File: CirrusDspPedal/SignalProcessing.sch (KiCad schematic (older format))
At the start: 8 parts, among them J3 Conn_02x05_Odd_Even, U4 STM32F411RETx

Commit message: Added Footswitches and relay
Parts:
- J3: footprint (none) -> Connector_PinHeader_2.54mm:PinHeader_2x05_P2.54mm_Vertical_SMD
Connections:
- net labels added: ExpInput, FootSwitchA, FootSwitchB, SIgnalSwitch
- wire segments 84 -> 90
- no-connect marks 44 -> 40
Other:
- moved on the sheet: C18, C19, C20, C21, C22, J3, L1

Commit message: Added UserPots and RGB LEDS
Updated schema docs
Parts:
- added LED1, LED2: LED_RABG, LED_THT:LED_D5.0mm-4_RGB_Wide_Pins, symbol Device:LED_RABG
- added R17, R18, R19, R20, R21, R22: 220R, Resistor_SMD:R_0805_2012Metric_Pad1.15x1.40mm_HandSolder, symbol Device:R
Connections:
- net labels added: LEDA_B, LEDA_G, LEDA_R, LEDB_B, LEDB_G, LEDB_R, UserPotA, UserPotB, UserSwA, UserSwB
- wire segments 90 -> 116
- no-connect marks 40 -> 30
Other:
- note added: "I2S_2_CK"
- note added: "I2S_2_Ext_SD"
- note added: "I2S_2_MCLK"
- note added: "I2S_2_SD"
- note added: "I2S_2_WS"
- moved on the sheet: C18, C19, C20, C21, C22, J3, L1

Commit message: Completed schematic design
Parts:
- removed U4: STM32F411RETx, Package_QFP:LQFP-64_10x10mm_P0.5mm, symbol MCU_ST_STM32F4:STM32F411RETx
- added C33: 2.2uF, Capacitor_SMD:C_0805_2012Metric_Pad1.15x1.40mm_HandSolder, symbol Device:C
- added U7: STM32F405RGTx, Package_QFP:LQFP-64_10x10mm_P0.5mm, symbol MCU_ST_STM32F4:STM32F405RGTx
- C22: value 100nF -> 2.2uF
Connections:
- net labels added: FootExp_IN, FootSwitchA_IN, FootSwitchB_IN, RelayCoil_OUT, UserPotA_IN, UserPotB_IN, UserSwitchB_IN, UserSwithA_IN, VCAP1, VCAP2, uSD_CLK, uSD_CMD, uSD_D0, uSD_D1, uSD_D2, uSD_D3, uSD_Detect
- net labels removed: ExpInput, FootSwitchA, FootSwitchB, SIgnalSwitch, UserPotA, UserPotB, UserSwA, UserSwB
- wire segments 116 -> 125
- no-connect marks 30 -> 24
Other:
- note added: "AnalogInput"
- note added: "DigitalInput"
- note added: "DigitalOutput"
- note added: "SDIO_CK"
- note added: "SDIO_CMD"
- note added: "SDIO_D0"
- note added: "SDIO_D1"
- note added: "SDIO_D2"
- note added: "SDIO_D3"
- note added: "SDIO_Detect"
- note added: "SYS_JTCK-SWCLK"
- note added: "SYS_JTDO-SWO"
- note added: "SYS_JTMS-SWDIO"
- moved on the sheet: C22

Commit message: updates
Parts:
- J3: footprint Connector_PinHeader_2.54mm:PinHeader_2x05_P2.54mm_Vertical_SMD -> Connector_PinHeader_1.27mm:PinHeader_2x05_P1.27mm_Vertical_SMD
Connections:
- net labels removed: VBAT
- wire segments 125 -> 121
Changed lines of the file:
@@
 $Descr A4 11693 8268
 encoding utf-8
-Sheet 8 11
+Sheet 8 10
 Title ""
 Date ""
@@
 Wire Wire Line
 	6350 1600 6350 1325
-Text Label 6125 1325 0    50   ~ 0
-VBAT
 Wire Wire Line
 	6600 1325 6600 1150
@@
 Wire Wire Line
 	5850 2000 4950 2000
-$Sheet
-S 1850 925  925  625
-U 5F89A953
-F0 "STM32F411_PowerFiltering" 50
-F1 "STM32F411_PowerFiltering.sch" 50
-F2 "VDDA" I R 2775 1125 50
-F3 "VBAT" I R 2775 1350 50
-F4 "VDD_IN" I L 1850 1125 50
-$EndSheet
-Text Label 3425 1350 0    50   ~ 0
-VBAT
-Wire Wire Line
-	2775 1350 3425 1350
-Text Label 3425 1125 0    50   ~ 0
-VDDA
-Wire Wire Line
-	2775 1125 3425 1125
-$Comp
-L power:+3.3V #PWR0118
-U 1 1 5F8C8E66
-P 1400 1000
-F 0 "#PWR0118" H 1400 850 50  0001 C CNN
-F 1 "+3.3V" H 1415 1173 50  0000 C CNN
-F 2 "" H 1400 1000 50  0001 C CNN
-F 3 "" H 1400 1000 50  0001 C CNN
-	1    1400 1000
-	1    0    0    -1
-$EndComp
-Wire Wire Line
-	1400 1125 1400 1000
-Wire Wire Line
-	1850 1125 1400 1125
 $Comp
 L Device:C C?
@@
 F 0 "J3" H 2375 3017 50  0000 C CNN
 F 1 "Conn_02x05_Odd_Even" H 2375 2926 50  0000 C CNN
-F 2 "Connector_PinHeader_2.54mm:PinHeader_2x05_P2.54mm_Vertical_SMD" H 2325 2600 50  0001 C CNN
-F 3 "~" H 2325 2600 50  0001 C CNN
+F 2 "Connector_PinHeader_1.27mm:PinHeader_2x05_P1.27mm_Vertical_SMD" H 2325 2600 50  0001 C CNN
+F 3 "https://docs.rs-online.com/75e3/0900766b8142184e.pdf" H 2325 2600 50  0001 C CNN
 	1    2325 2600
 	1    0    0    -1
@@
 	6850 1325 7075 1325
 Wire Wire Line
-	6350 1325 6125 1325
+	6350 1325 6450 1325
 Wire Wire Line
 	7250 1800 7950 1800
@@
 Text Notes 7375 2600 0    50   ~ 0
 SDIO_Detect
+Connection ~ 6450 1325
 $EndSCHEMATC

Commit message: updated design and layout
- Changed LDO to 1703 (footprint unchanged)
- Changed THT LEDs from RAGB (incorrect) to RCGB (correct) symbol (footprint unchanged)
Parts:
- removed LED1, LED2: LED_RABG, LED_THT:LED_D5.0mm-4_RGB_Wide_Pins, symbol Device:LED_RABG
- added LED1, LED2: LED_RCBG, LED_THT:LED_D5.0mm-4_RGB_Wide_Pins, symbol Device:LED_RCBG
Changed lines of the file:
@@
 Text HLabel 7950 2000 2    50   Input ~ 0
 UserPotB_IN
-$Comp
-L Device:LED_RABG LED1
-U 1 1 5F968A63
-P 10000 2450
-F 0 "LED1" H 10000 2947 50  0000 C CNN
-F 1 "LED_RABG" H 10000 2856 50  0000 C CNN
-F 2 "LED_THT:LED_D5.0mm-4_RGB_Wide_Pins" H 10000 2400 50  0001 C CNN
-F 3 "~" H 10000 2400 50  0001 C CNN
-	1    10000 2450
-	1    0    0    -1
-$EndComp
 Wire Wire Line
 	9800 2250 9700 2250
@@
 Text Label 9050 2650 0    50   ~ 0
 LEDA_B
-$Comp
-L Device:LED_RABG LED2
-U 1 1 5F8E8343
-P 10000 3650
-F 0 "LED2" H 10000 4147 50  0000 C CNN
-F 1 "LED_RABG" H 10000 4056 50  0000 C CNN
-F 2 "LED_THT:LED_D5.0mm-4_RGB_Wide_Pins" H 10000 3600 50  0001 C CNN
-F 3 "~" H 10000 3600 50  0001 C CNN
-	1    10000 3650
-	1    0    0    -1
-$EndComp
 Wire Wire Line
 	9800 3450 9700 3450
@@
 SDIO_Detect
 Connection ~ 6450 1325
+$Comp
+L Device:LED_RCBG LED1
+U 1 1 5F9CA392
+P 10000 2450
+F 0 "LED1" H 10000 2947 50  0000 C CNN
+F 1 "LED_RCBG" H 10000 2856 50  0000 C CNN
+F 2 "LED_THT:LED_D5.0mm-4_RGB_Wide_Pins" H 10000 2400 50  0001 C CNN
+F 3 "~" H 10000 2400 50  0001 C CNN
+	1    10000 2450
+	-1   0    0    -1
+$EndComp
+$Comp
+L Device:LED_RCBG LED2
+U 1 1 5F9CDB3E
+P 10000 3650
+F 0 "LED2" H 10000 4147 50  0000 C CNN
+F 1 "LED_RCBG" H 10000 4056 50  0000 C CNN
+F 2 "LED_THT:LED_D5.0mm-4_RGB_Wide_Pins" H 10000 3600 50  0001 C CNN
+F 3 "~" H 10000 3600 50  0001 C CNN
+	1    10000 3650
+	-1   0    0    -1
+$EndComp
 $EndSCHEMATC

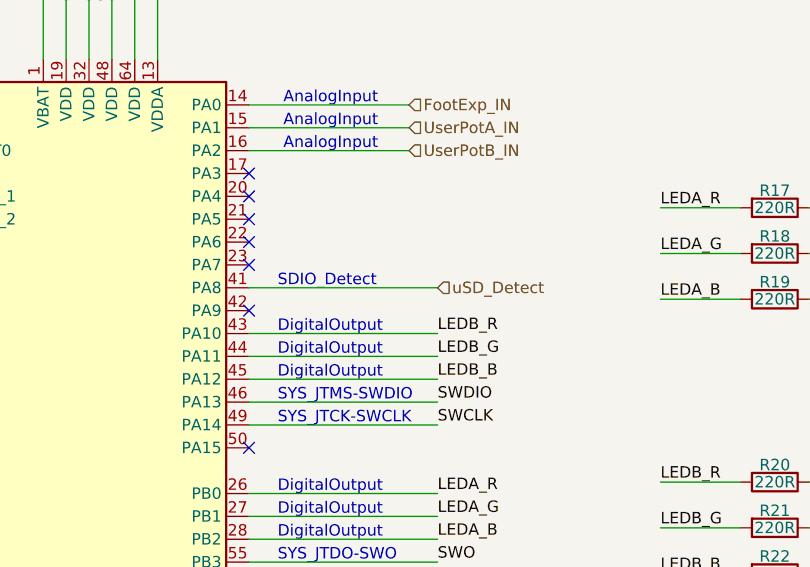
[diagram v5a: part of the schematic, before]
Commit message: replaced SDIO connector
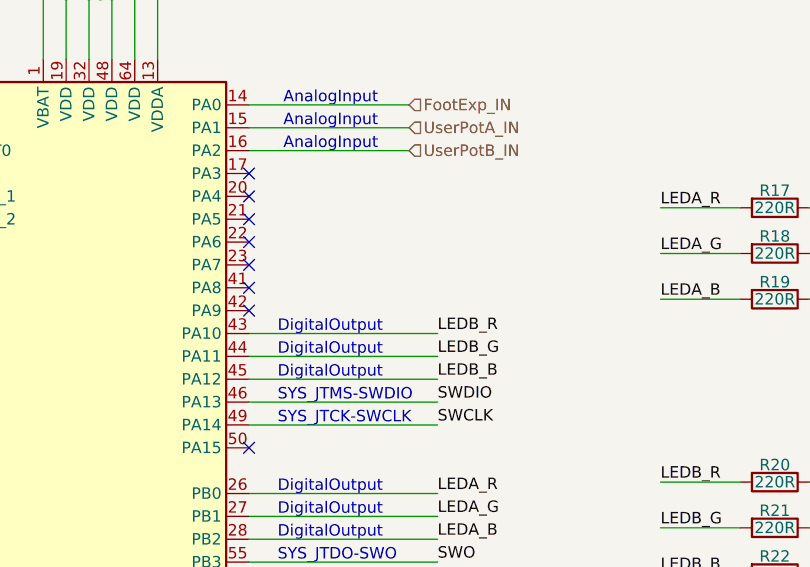
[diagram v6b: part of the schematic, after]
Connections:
- net uSD_Detect: no longer names the net of U7.41 (PA8)
- no-connect marks 24 -> 25
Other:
- note removed: "SDIO_Detect"
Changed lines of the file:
@@
 Text HLabel 5100 4600 0    50   Input ~ 0
 uSD_D3
-Wire Wire Line
-	7250 2600 8075 2600
-Text HLabel 8075 2600 2    50   Input ~ 0
-uSD_Detect
-Text Notes 7375 2600 0    50   ~ 0
-SDIO_Detect
 Connection ~ 6450 1325
 $Comp
@@
 	-1   0    0    -1
 $EndComp
+NoConn ~ 7250 2600
 $EndSCHEMATC

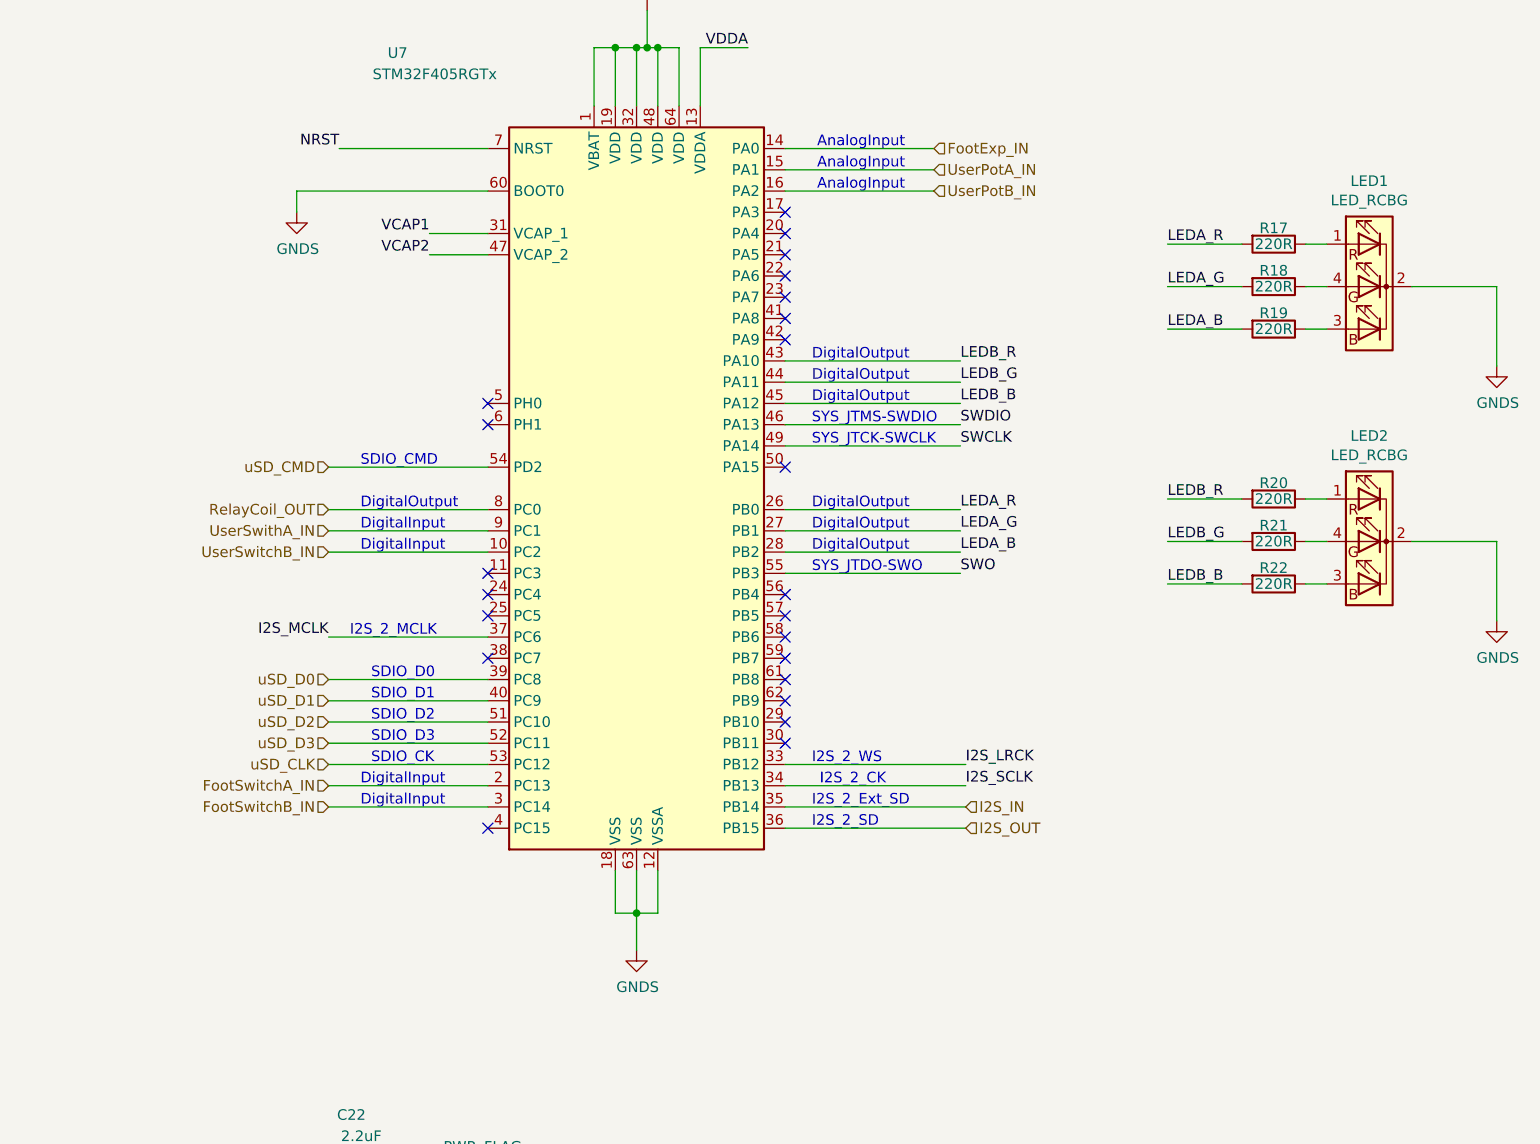
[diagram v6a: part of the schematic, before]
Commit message: Updated RevB
- Replaced analog pots with Rotary Encoders
- Added I2C connector (for OLED screen)
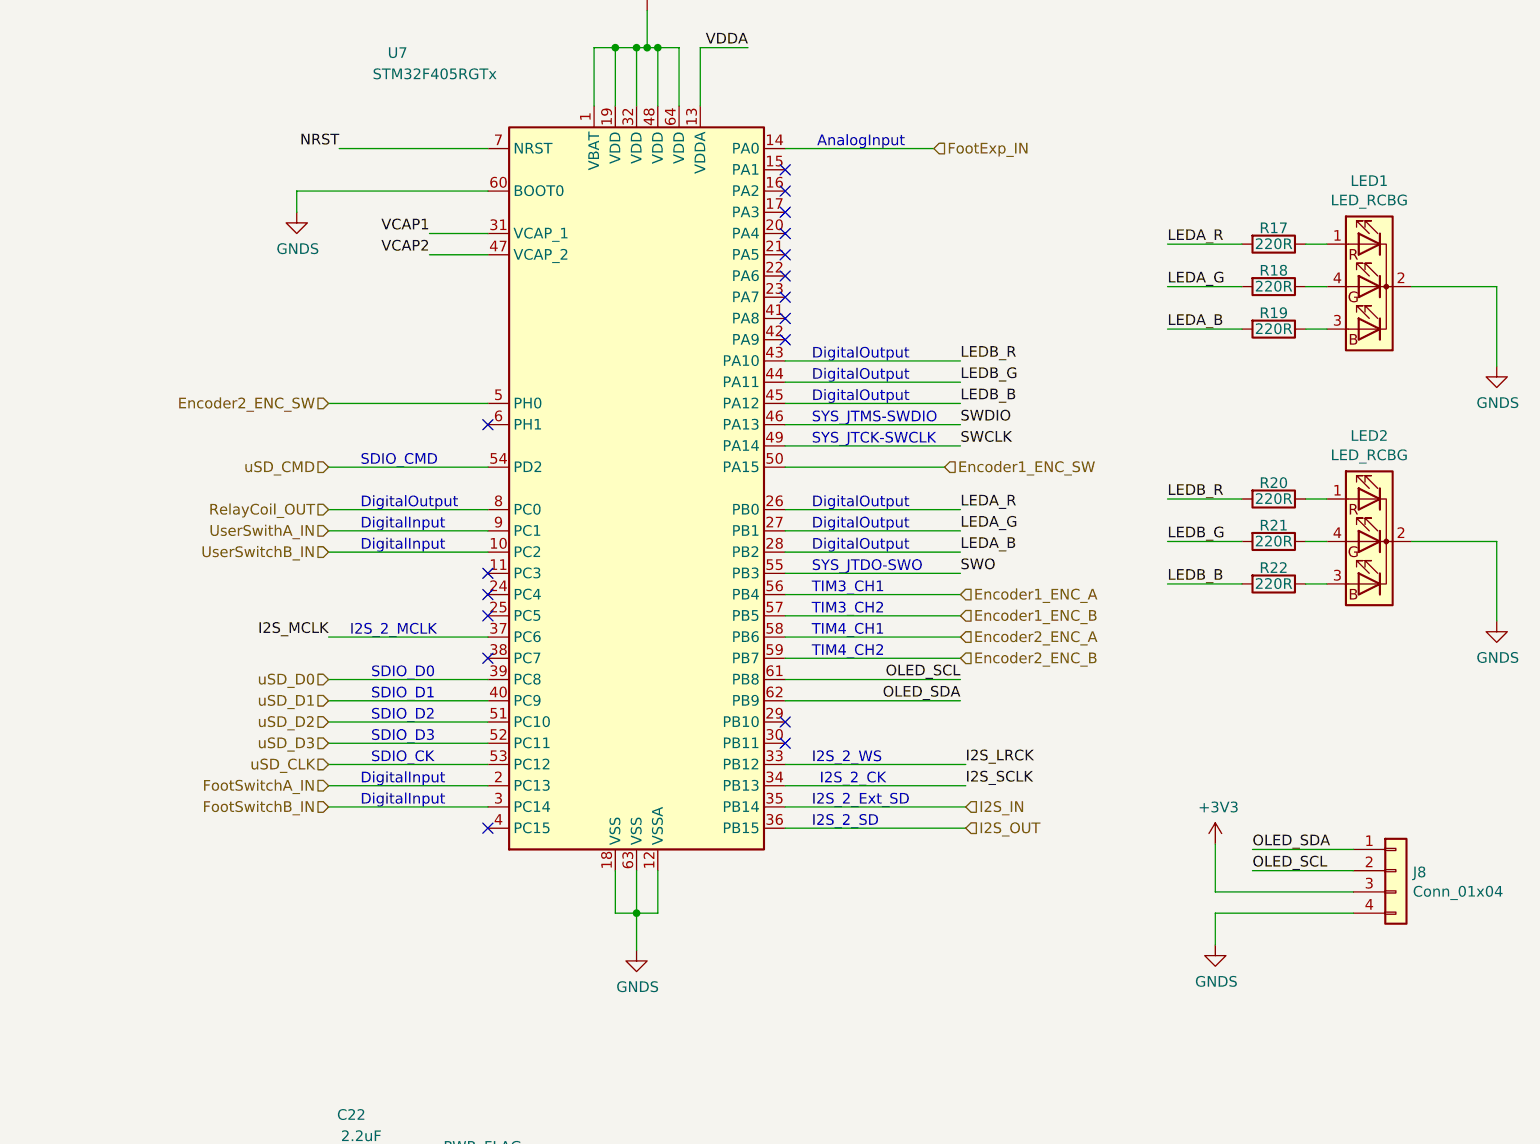
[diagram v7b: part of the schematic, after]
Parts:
- added J8: Conn_01x04, Connector_Molex:Molex_KK-254_AE-6410-04A_1x04_P2.54mm_Vertical, symbol Connector_Generic:Conn_01x04
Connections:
- net +3V3: now also J8.3 (Pin_3)
- net GNDS: now also J8.4 (Pin_4)
- net Encoder2_ENC_SW: now reaches U7.5 (PH0)
- net Encoder1_ENC_SW: now reaches U7.50 (PA15)
- net Encoder1_ENC_A: now reaches U7.56 (PB4)
- net Encoder1_ENC_B: now reaches U7.57 (PB5)
- net Encoder2_ENC_A: now reaches U7.58 (PB6)
- net Encoder2_ENC_B: now reaches U7.59 (PB7)
- net OLED_SCL: now reaches U7.61 (PB8)
- net OLED_SCL: now also J8.2 (Pin_2)
- net OLED_SDA: now reaches U7.62 (PB9)
- net OLED_SDA: now also J8.1 (Pin_1)
- net UserPotA_IN: no longer names the net of U7.15 (PA1)
- net UserPotB_IN: no longer names the net of U7.16 (PA2)
- no-connect marks 25 -> 19
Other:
- note added: "TIM3_CH1"
- note added: "TIM3_CH2\n"
- note added: "TIM4_CH1"
- note added: "TIM4_CH2"
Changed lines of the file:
@@
 $Descr A4 11693 8268
 encoding utf-8
-Sheet 8 10
+Sheet 8 12
 Title ""
 Date ""
@@
 Text HLabel 2725 3800 2    50   Input ~ 0
 I2S_SCLK_OUT
-NoConn ~ 5850 3000
 NoConn ~ 5850 3900
 NoConn ~ 5850 4000
 NoConn ~ 7250 4500
 NoConn ~ 5850 3800
-NoConn ~ 7250 4400
-NoConn ~ 7250 4300
-NoConn ~ 7250 4200
-NoConn ~ 7250 4100
-NoConn ~ 7250 4000
-NoConn ~ 7250 3900
-NoConn ~ 7250 3300
 NoConn ~ 7250 2700
 NoConn ~ 7250 2500
@@
 Text HLabel 7950 1800 2    50   Input ~ 0
 FootExp_IN
-Wire Wire Line
-	7250 1900 7950 1900
-Text HLabel 7950 1900 2    50   Input ~ 0
-UserPotA_IN
-Wire Wire Line
-	7250 2000 7950 2000
-Text HLabel 7950 2000 2    50   Input ~ 0
-UserPotB_IN
 Wire Wire Line
 	9800 2250 9700 2250
@@
 DigitalInput
 Text Notes 7400 1800 0    50   ~ 0
-AnalogInput
-Text Notes 7400 1900 0    50   ~ 0
-AnalogInput
-Text Notes 7400 2000 0    50   ~ 0
 AnalogInput
 Text Notes 7375 2800 0    50   ~ 0
@@
 $EndComp
 NoConn ~ 7250 2600
+Wire Wire Line
+	7250 3900 8075 3900
+Text HLabel 8075 3900 2    50   Input ~ 0
+Encoder1_ENC_A
+Text Notes 7375 3900 0    50   ~ 0
+TIM3_CH1
+Text Notes 7375 4000 0    50   ~ 0
+TIM3_CH2\n
+Wire Wire Line
+	7250 4000 8075 4000
+Text HLabel 8075 4000 2    50   Input ~ 0
+Encoder1_ENC_B
+Wire Wire Line
+	7250 4100 8075 4100
+Wire Wire Line
+	7250 4200 8075 4200
+Text Notes 7375 4100 0    50   ~ 0
+TIM4_CH1
+Text Notes 7375 4200 0    50   ~ 0
+TIM4_CH2
+Text HLabel 8075 4100 2    50   Input ~ 0
+Encoder2_ENC_A
+Text HLabel 8075 4200 2    50   Input ~ 0
+Encoder2_ENC_B
+NoConn ~ 7250 1900
+NoConn ~ 7250 2000
+$Comp
+L Connector_Generic:Conn_01x04 J8
+U 1 1 5FB31B5E
+P 10125 5200
+F 0 "J8" H 10205 5192 50  0000 L CNN
+F 1 "Conn_01x04" H 10205 5101 50  0000 L CNN
+F 2 "Connector_Molex:Molex_KK-254_AE-6410-04A_1x04_P2.54mm_Vertical" H 10125 5200 50  0001 C CNN
+F 3 "~" H 10125 5200 50  0001 C CNN
+	1    10125 5200
+	1    0    0    -1
+$EndComp
+Wire Wire Line
+	7250 4300 8075 4300
+Text Label 8075 4400 2    50   ~ 0
+OLED_SDA
+Wire Wire Line
+	7250 4400 8075 4400
+Text Label 8075 4300 2    50   ~ 0
+OLED_SCL
+Wire Wire Line
+	9925 5200 9450 5200
+Text Label 9450 5100 0    50   ~ 0
+OLED_SDA
+Wire Wire Line
+	9925 5100 9450 5100
+Text Label 9450 5200 0    50   ~ 0
+OLED_SCL
+Wire Wire Line
+	9925 5300 9275 5300
+Wire Wire Line
+	9275 5300 9275 5075
+$Comp
+L power:+3V3 #PWR06
+U 1 1 5FB526D6
+P 9275 5075
+F 0 "#PWR06" H 9275 4925 50  0001 C CNN
+F 1 "+3V3" H 9290 5248 50  0000 C CNN
+F 2 "" H 9275 5075 50  0001 C CNN
+F 3 "" H 9275 5075 50  0001 C CNN
+	1    9275 5075
+	1    0    0    -1
+$EndComp
+Wire Wire Line
+	9925 5400 9275 5400
+Wire Wire Line
+	9275 5400 9275 5550
+$Comp
+L power:GNDS #PWR07
+U 1 1 5FB58162
+P 9275 5550
+F 0 "#PWR07" H 9275 5300 50  0001 C CNN
+F 1 "GNDS" H 9280 5377 50  0000 C CNN
+F 2 "" H 9275 5550 50  0001 C CNN
+F 3 "" H 9275 5550 50  0001 C CNN
+	1    9275 5550
+	1    0    0    -1
+$EndComp
+Wire Wire Line
+	5850 3000 5100 3000
+Text HLabel 5100 3000 0    50   Input ~ 0
+Encoder2_ENC_SW
+Wire Wire Line
+	7250 3300 8000 3300
+Text HLabel 8000 3300 2    50   Input ~ 0
+Encoder1_ENC_SW
 $EndSCHEMATC

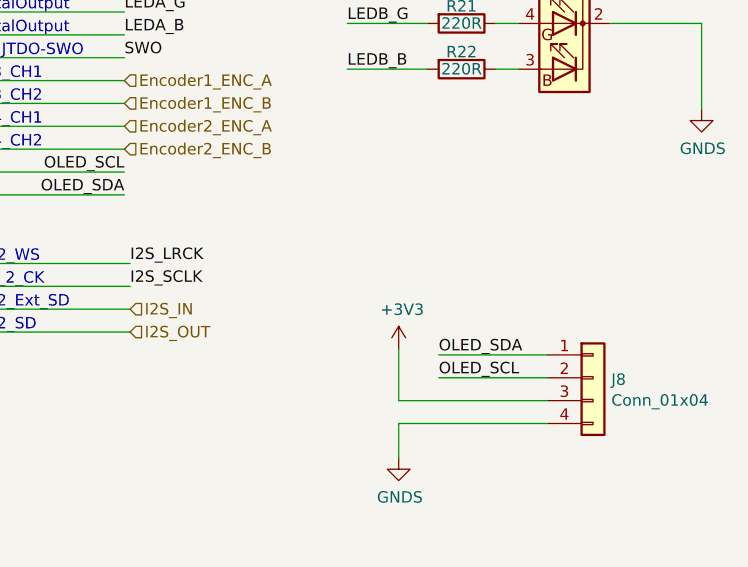
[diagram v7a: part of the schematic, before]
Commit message: updated revB
- Added higher out current LDO (LD1117) for 5V rail
- Added jumper on OLED connector to select 3V3/5V
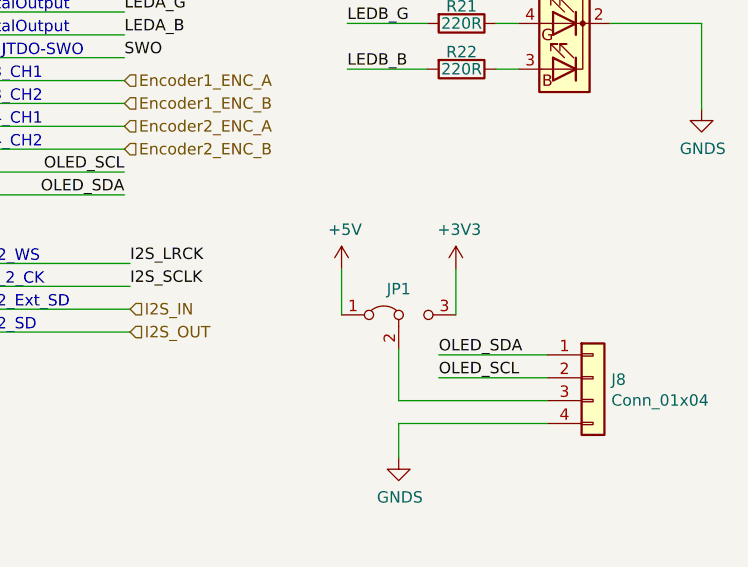
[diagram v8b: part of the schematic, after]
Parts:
- added JP1: Jumper_3_Bridged12, Jumper:SolderJumper-3_P1.3mm_Bridged2Bar12_Pad1.0x1.5mm, symbol Jumper:Jumper_3_Bridged12
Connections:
- net +3V3: now also JP1.3 (B); no longer J8.3 (Pin_3)
- new net: J8.3 (Pin_3), JP1.2 (C)
- new net +5V: JP1.1 (A)
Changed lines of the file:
@@
 Wire Wire Line
 	9275 5300 9275 5075
-$Comp
-L power:+3V3 #PWR06
-U 1 1 5FB526D6
-P 9275 5075
-F 0 "#PWR06" H 9275 4925 50  0001 C CNN
-F 1 "+3V3" H 9290 5248 50  0000 C CNN
-F 2 "" H 9275 5075 50  0001 C CNN
-F 3 "" H 9275 5075 50  0001 C CNN
-	1    9275 5075
-	1    0    0    -1
-$EndComp
 Wire Wire Line
 	9925 5400 9275 5400
@@
 Text HLabel 8000 3300 2    50   Input ~ 0
 Encoder1_ENC_SW
+$Comp
+L Jumper:Jumper_3_Bridged12 JP1
+U 1 1 5FAD494A
+P 9275 4925
+F 0 "JP1" H 9275 5038 50  0000 C CNN
+F 1 "Jumper_3_Bridged12" H 9275 5038 50  0001 C CNN
+F 2 "Jumper:SolderJumper-3_P1.3mm_Bridged2Bar12_Pad1.0x1.5mm" H 9275 4925 50  0001 C CNN
+F 3 "~" H 9275 4925 50  0001 C CNN
+	1    9275 4925
+	1    0    0    -1
+$EndComp
+$Comp
+L power:+3V3 #PWR0142
+U 1 1 5FAD5633
+P 9525 4725
+F 0 "#PWR0142" H 9525 4575 50  0001 C CNN
+F 1 "+3V3" H 9540 4898 50  0000 C CNN
+F 2 "" H 9525 4725 50  0001 C CNN
+F 3 "" H 9525 4725 50  0001 C CNN
+	1    9525 4725
+	1    0    0    -1
+$EndComp
+$Comp
+L power:+5V #PWR0143
+U 1 1 5FAD631E
+P 9025 4725
+F 0 "#PWR0143" H 9025 4575 50  0001 C CNN
+F 1 "+5V" H 9040 4898 50  0000 C CNN
+F 2 "" H 9025 4725 50  0001 C CNN
+F 3 "" H 9025 4725 50  0001 C CNN
+	1    9025 4725
+	1    0    0    -1
+$EndComp
+Wire Wire Line
+	9025 4725 9025 4925
+Wire Wire Line
+	9525 4925 9525 4725
 $EndSCHEMATC
